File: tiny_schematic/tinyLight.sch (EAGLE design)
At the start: 36 parts, among them IC1 NCP1117, IC2 XMEGA-A4TQFP, IC3 CM1293A-02SR, J1 RASM722PX, J2 Molex, J3 PDI, Q1 BC849SMD, Q2 BC849SMD, X1 MICRO-USB

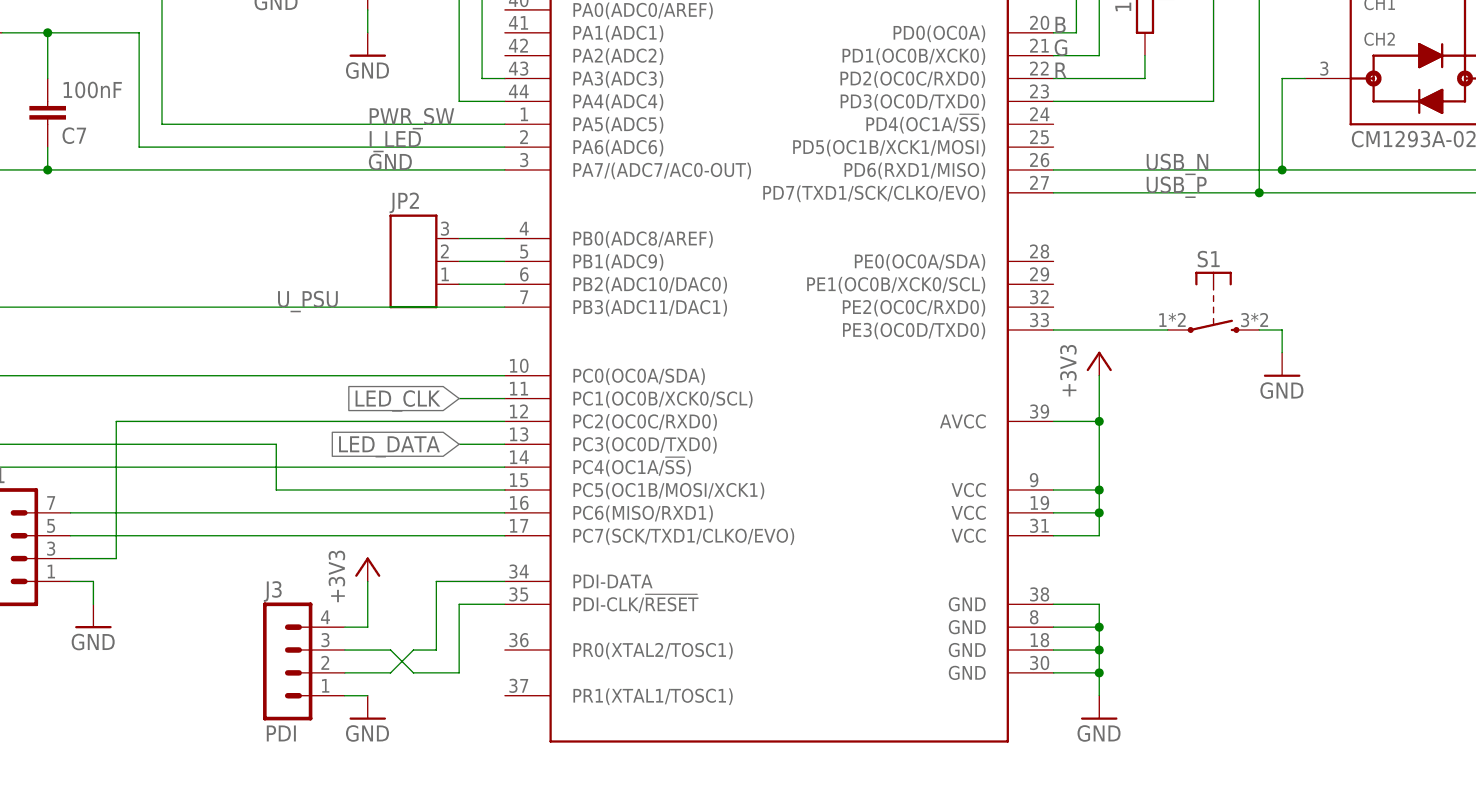
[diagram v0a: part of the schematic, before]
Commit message: Added Uart and Ir-Header
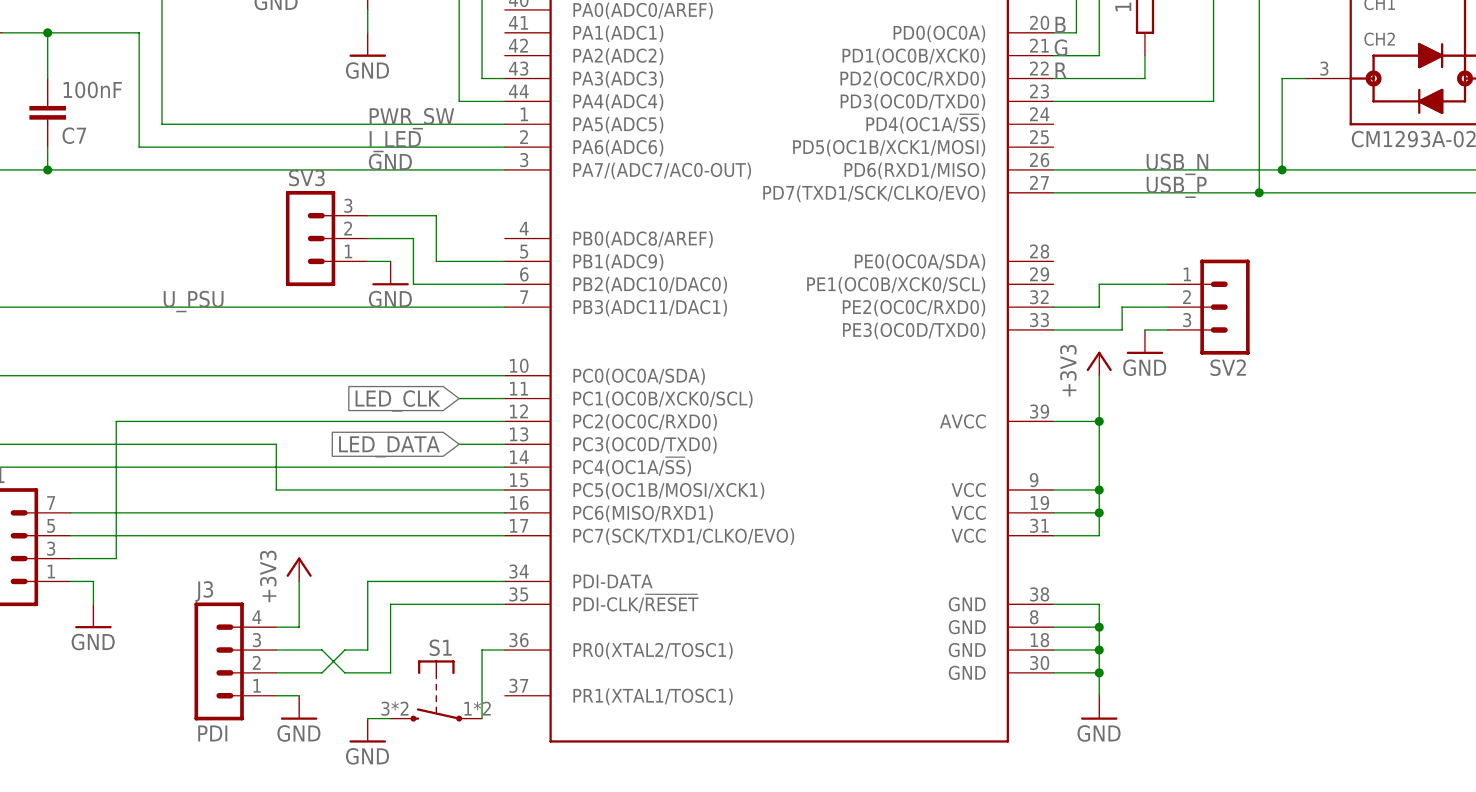
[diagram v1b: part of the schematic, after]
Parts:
- removed JP2: SMD_3PIN, tinyLight:SMD_3PIN
- added SV2, SV3: (no value), con-lstb:MA03-1
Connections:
- removed net N$1: IC2.PB0(ADC8/AREF), JP2.P$3
- removed net PB: IC2.PE3(OC0D/TXD0), S1.1
- new net N$10: IC2.PE3(OC0D/TXD0), SV2.2
- new net N$11: IC2.PE2(OC0C/RXD0), SV2.1
- new net N$12: IC2.PR0(XTAL2/TOSC1), S1.1
- net GND: now also SV2.3, SV3.1
- net N$2: now also SV3.2; no longer JP2.P$1
- net N$27: now also SV3.3; no longer JP2.P$2
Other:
- moved on the sheet: J3, S1
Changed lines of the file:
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@@
 <part name="GND5" library="supply1" deviceset="GND" device=""/>
 <part name="+3V5" library="supply1" deviceset="+3V3" device=""/>
-<part name="JP2" library="tinyLight" deviceset="SMD_3PIN" device=""/>
 <part name="+3V6" library="supply1" deviceset="+3V3" device=""/>
 <part name="R4" library="rcl" deviceset="R-EU_" device="M2012" value="5.6k"/>
@@
 <part name="C9" library="rcl" deviceset="C-EU" device="C2012" value="100nF"/>
 <part name="SV1" library="con-lstb" deviceset="MA04-2" device=""/>
+<part name="SV2" library="con-lstb" deviceset="MA03-1" device=""/>
+<part name="GND16" library="supply1" deviceset="GND" device=""/>
+<part name="SV3" library="con-lstb" deviceset="MA03-1" device=""/>
+<part name="GND17" library="supply1" deviceset="GND" device=""/>
 </parts>
 <sheets>
@@
 <instance part="GND8" gate="1" x="78.74" y="86.36"/>
 <instance part="Q3" gate="G$1" x="35.56" y="109.22" rot="MR0"/>
-<instance part="J3" gate="1" x="78.74" y="12.7"/>
-<instance part="GND7" gate="1" x="88.9" y="5.08"/>
+<instance part="J3" gate="1" x="71.12" y="12.7"/>
+<instance part="GND7" gate="1" x="81.28" y="5.08"/>
 <instance part="C6" gate="G$1" x="208.28" y="121.92" rot="R180"/>
-<instance part="GND9" gate="1" x="190.5" y="43.18"/>
+<instance part="GND9" gate="1" x="88.9" y="2.54"/>
 <instance part="R10" gate="G$1" x="251.46" y="93.98" rot="R270"/>
 <instance part="GND10" gate="1" x="251.46" y="83.82"/>
@@
 <instance part="GND5" gate="1" x="58.42" y="15.24"/>
 <instance part="+3V5" gate="G$1" x="30.48" y="25.4"/>
-<instance part="JP2" gate="G$1" x="93.98" y="55.88"/>
-<instance part="+3V6" gate="G$1" x="88.9" y="22.86"/>
+<instance part="+3V6" gate="G$1" x="81.28" y="22.86"/>
 <instance part="R4" gate="G$1" x="53.34" y="99.06" rot="R270"/>
 <instance part="P+5" gate="1" x="45.72" y="160.02"/>
@@
 <instance part="P+8" gate="1" x="231.14" y="93.98"/>
 <instance part="P+9" gate="1" x="251.46" y="119.38"/>
-<instance part="S1" gate="G$1" x="182.88" y="48.26"/>
+<instance part="S1" gate="G$1" x="96.52" y="5.08" rot="MR0"/>
 <instance part="C9" gate="G$1" x="25.4" y="43.18"/>
 <instance part="SV1" gate="G$1" x="48.26" y="25.4"/>
+<instance part="SV2" gate="G$1" x="185.42" y="50.8" rot="R180"/>
+<instance part="GND16" gate="1" x="175.26" y="45.72"/>
+<instance part="SV3" gate="G$1" x="81.28" y="58.42"/>
+<instance part="GND17" gate="1" x="91.44" y="53.34"/>
 </instances>
 <busses>
@@
 <pinref part="J3" gate="1" pin="1"/>
 <pinref part="GND7" gate="1" pin="GND"/>
-<wire x1="88.9" y1="7.62" x2="86.36" y2="7.62" width="0.1524" layer="91"/>
+<wire x1="81.28" y1="7.62" x2="78.74" y2="7.62" width="0.1524" layer="91"/>
 </segment>
 <segment>
 <pinref part="GND9" gate="1" pin="GND"/>
-<wire x1="190.5" y1="45.72" x2="190.5" y2="48.26" width="0.1524" layer="91"/>
 <pinref part="S1" gate="G$1" pin="2"/>
-<wire x1="187.96" y1="48.26" x2="190.5" y2="48.26" width="0.1524" layer="91"/>
+<wire x1="91.44" y1="5.08" x2="88.9" y2="5.08" width="0.1524" layer="91"/>
 </segment>
 <segment>
@@
 <pinref part="SV1" gate="G$1" pin="1"/>
 <wire x1="55.88" y1="20.32" x2="58.42" y2="20.32" width="0.1524" layer="91"/>
+</segment>
+<segment>
+<pinref part="GND16" gate="1" pin="GND"/>
+<pinref part="SV2" gate="G$1" pin="3"/>
+<wire x1="175.26" y1="48.26" x2="177.8" y2="48.26" width="0.1524" layer="91"/>
+</segment>
+<segment>
+<pinref part="SV3" gate="G$1" pin="1"/>
+<pinref part="GND17" gate="1" pin="GND"/>
+<wire x1="88.9" y1="55.88" x2="91.44" y2="55.88" width="0.1524" layer="91"/>
 </segment>
 </net>
@@
 <pinref part="J3" gate="1" pin="4"/>
 <pinref part="+3V6" gate="G$1" pin="+3V3"/>
-<wire x1="86.36" y1="15.24" x2="88.9" y2="15.24" width="0.1524" layer="91"/>
-<wire x1="88.9" y1="15.24" x2="88.9" y2="20.32" width="0.1524" layer="91"/>
+<wire x1="78.74" y1="15.24" x2="81.28" y2="15.24" width="0.1524" layer="91"/>
+<wire x1="81.28" y1="15.24" x2="81.28" y2="20.32" width="0.1524" layer="91"/>
 </segment>
 <segment>
@@
 <junction x="15.24" y="50.8"/>
 <wire x1="15.24" y1="50.8" x2="15.24" y2="53.34" width="0.1524" layer="91"/>
-<label x="78.74" y="50.8" size="1.778" layer="95"/>
+<label x="66.04" y="50.8" size="1.778" layer="95"/>
 <pinref part="C9" gate="G$1" pin="1"/>
 <wire x1="25.4" y1="45.72" x2="25.4" y2="50.8" width="0.1524" layer="91"/>
@@
 <segment>
 <pinref part="J3" gate="1" pin="3"/>
-<wire x1="86.36" y1="12.7" x2="91.44" y2="12.7" width="0.1524" layer="91"/>
-<wire x1="91.44" y1="12.7" x2="93.98" y2="10.16" width="0.1524" layer="91"/>
+<wire x1="78.74" y1="12.7" x2="83.82" y2="12.7" width="0.1524" layer="91"/>
+<wire x1="83.82" y1="12.7" x2="86.36" y2="10.16" width="0.1524" layer="91"/>
 <pinref part="IC2" gate="G$1" pin="PDI-CLK/!RESET"/>
-<wire x1="93.98" y1="10.16" x2="99.06" y2="10.16" width="0.1524" layer="91"/>
-<wire x1="99.06" y1="10.16" x2="99.06" y2="17.78" width="0.1524" layer="91"/>
-<wire x1="99.06" y1="17.78" x2="104.14" y2="17.78" width="0.1524" layer="91"/>
+<wire x1="86.36" y1="10.16" x2="91.44" y2="10.16" width="0.1524" layer="91"/>
+<wire x1="91.44" y1="10.16" x2="91.44" y2="17.78" width="0.1524" layer="91"/>
+<wire x1="91.44" y1="17.78" x2="104.14" y2="17.78" width="0.1524" layer="91"/>
 </segment>
 </net>
@@
 <segment>
 <pinref part="IC2" gate="G$1" pin="PDI-DATA"/>
-<wire x1="104.14" y1="20.32" x2="96.52" y2="20.32" width="0.1524" layer="91"/>
-<wire x1="96.52" y1="20.32" x2="96.52" y2="12.7" width="0.1524" layer="91"/>
-<wire x1="96.52" y1="12.7" x2="93.98" y2="12.7" width="0.1524" layer="91"/>
-<wire x1="93.98" y1="12.7" x2="91.44" y2="10.16" width="0.1524" layer="91"/>
+<wire x1="104.14" y1="20.32" x2="88.9" y2="20.32" width="0.1524" layer="91"/>
+<wire x1="88.9" y1="20.32" x2="88.9" y2="12.7" width="0.1524" layer="91"/>
+<wire x1="88.9" y1="12.7" x2="86.36" y2="12.7" width="0.1524" layer="91"/>
+<wire x1="86.36" y1="12.7" x2="83.82" y2="10.16" width="0.1524" layer="91"/>
 <pinref part="J3" gate="1" pin="2"/>
-<wire x1="91.44" y1="10.16" x2="86.36" y2="10.16" width="0.1524" layer="91"/>
+<wire x1="83.82" y1="10.16" x2="78.74" y2="10.16" width="0.1524" layer="91"/>
 </segment>
 </net>
@@
 </segment>
 </net>
-<net name="PB" class="0">
-<segment>
-<pinref part="IC2" gate="G$1" pin="PE3(OC0D/TXD0)"/>
-<wire x1="177.8" y1="48.26" x2="165.1" y2="48.26" width="0.1524" layer="91"/>
-<pinref part="S1" gate="G$1" pin="1"/>
-</segment>
-</net>
 <net name="N$27" class="0">
 <segment>
 <pinref part="IC2" gate="G$1" pin="PB1(ADC9)"/>
-<pinref part="JP2" gate="G$1" pin="P$2"/>
-<wire x1="99.06" y1="55.88" x2="104.14" y2="55.88" width="0.1524" layer="91"/>
+<wire x1="96.52" y1="55.88" x2="104.14" y2="55.88" width="0.1524" layer="91"/>
+<pinref part="SV3" gate="G$1" pin="3"/>
+<wire x1="88.9" y1="60.96" x2="96.52" y2="60.96" width="0.1524" layer="91"/>
+<wire x1="96.52" y1="60.96" x2="96.52" y2="55.88" width="0.1524" layer="91"/>
 </segment>
 </net>
@@
 </segment>
 </net>
-<net name="N$1" class="0">
-<segment>
-<pinref part="JP2" gate="G$1" pin="P$3"/>
-<pinref part="IC2" gate="G$1" pin="PB0(ADC8/AREF)"/>
-<wire x1="99.06" y1="58.42" x2="104.14" y2="58.42" width="0.1524" layer="91"/>
-</segment>
-</net>
 <net name="N$2" class="0">
 <segment>
 <pinref part="IC2" gate="G$1" pin="PB2(ADC10/DAC0)"/>
-<pinref part="JP2" gate="G$1" pin="P$1"/>
-<wire x1="104.14" y1="53.34" x2="99.06" y2="53.34" width="0.1524" layer="91"/>
+<pinref part="SV3" gate="G$1" pin="2"/>
+<wire x1="88.9" y1="58.42" x2="93.98" y2="58.42" width="0.1524" layer="91"/>
+<wire x1="93.98" y1="58.42" x2="93.98" y2="53.34" width="0.1524" layer="91"/>
+<wire x1="93.98" y1="53.34" x2="104.14" y2="53.34" width="0.1524" layer="91"/>
 </segment>
 </net>
@@
 </segment>
 </net>
+<net name="N$12" class="0">
+<segment>
+<pinref part="IC2" gate="G$1" pin="PR0(XTAL2/TOSC1)"/>
+<pinref part="S1" gate="G$1" pin="1"/>
+<wire x1="104.14" y1="12.7" x2="101.6" y2="12.7" width="0.1524" layer="91"/>
+<wire x1="101.6" y1="12.7" x2="101.6" y2="5.08" width="0.1524" layer="91"/>
+</segment>
+</net>
+<net name="N$10" class="0">
+<segment>
+<pinref part="IC2" gate="G$1" pin="PE3(OC0D/TXD0)"/>
+<wire x1="165.1" y1="48.26" x2="172.72" y2="48.26" width="0.1524" layer="91"/>
+<wire x1="172.72" y1="48.26" x2="172.72" y2="50.8" width="0.1524" layer="91"/>
+<pinref part="SV2" gate="G$1" pin="2"/>
+<wire x1="172.72" y1="50.8" x2="177.8" y2="50.8" width="0.1524" layer="91"/>
+</segment>
+</net>
+<net name="N$11" class="0">
+<segment>
+<pinref part="IC2" gate="G$1" pin="PE2(OC0C/RXD0)"/>
+<wire x1="165.1" y1="50.8" x2="170.18" y2="50.8" width="0.1524" layer="91"/>
+<wire x1="170.18" y1="50.8" x2="170.18" y2="53.34" width="0.1524" layer="91"/>
+<pinref part="SV2" gate="G$1" pin="1"/>
+<wire x1="170.18" y1="53.34" x2="177.8" y2="53.34" width="0.1524" layer="91"/>
+</segment>
+</net>

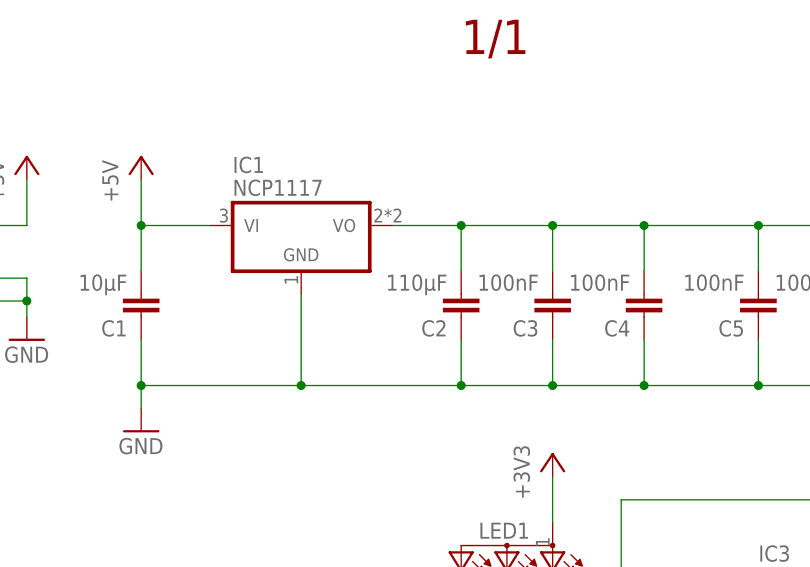
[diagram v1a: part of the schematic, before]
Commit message: bootloader ported to new hardware
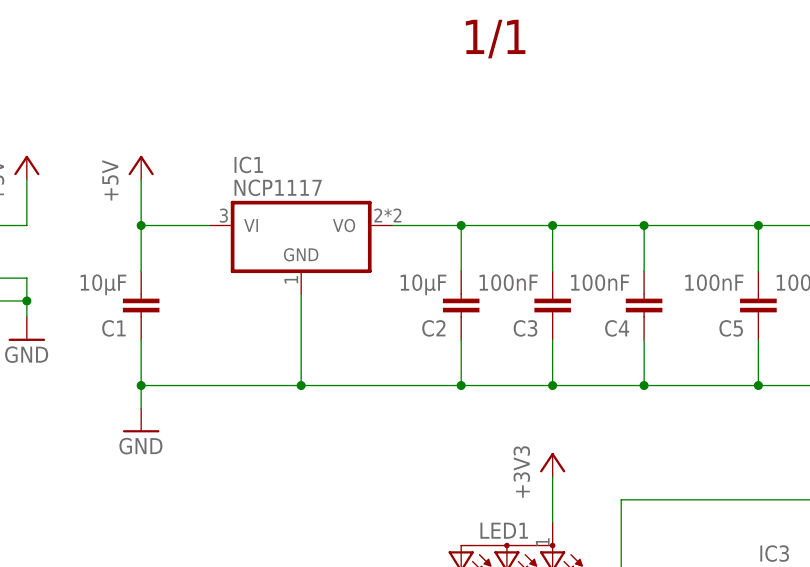
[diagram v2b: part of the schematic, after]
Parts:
- C2: value 110µF -> 10µF
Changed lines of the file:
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@@
 <part name="GND4" library="supply1" deviceset="GND" device=""/>
 <part name="C1" library="rcl" deviceset="C-EU" device="C2012" value="10µF"/>
-<part name="C2" library="rcl" deviceset="C-EU" device="C2012" value="110µF"/>
+<part name="C2" library="rcl" deviceset="C-EU" device="C2012" value="10µF"/>
 <part name="P+1" library="supply1" deviceset="+5V" device=""/>
 <part name="GND1" library="supply1" deviceset="GND" device=""/>
